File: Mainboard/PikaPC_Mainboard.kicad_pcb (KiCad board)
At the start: 2 copper layers, 190.5 x 147.3 mm, 67 parts, among them J10 Conn_01x08, J11 Conn_01x08, J12 Conn_01x08, J13 Conn_01x08, J14 Conn_01x08, J15 Conn_01x08, J16 Conn_01x08, J17 Conn_01x08, J18 Conn_01x10, J19 Conn_02x05_Odd_Even, J5 DIN41612_03x32_C_Split, J9 Conn_01x08, SW1 SW_Push_DPDT, SW2 SW_Push, U1 PPC403GA, U10 74LS07, U101 SN74LVC245A, U102 SN74LVC245A, U103 SN74LVC245A, U104 SN74LVC245A, U105 SN74LVC245A, U106 SN74LVC245A, U107 SN74LVC245A, U108 SN74LVC245A, U109 74LS244, U110 74LS244, U111 74LS244, U112 74LS244, U12 GD75232N, U13 74LVC125, U14 MCP120-315GI/TO, U15 AS6C4008-55PCN, U16 AS6C4008-55PCN, U2 ATF1508AS, U3 SST39VF010, U4 74AHCT244, U9 74LS04, Y1 25M, Y2 7M3728

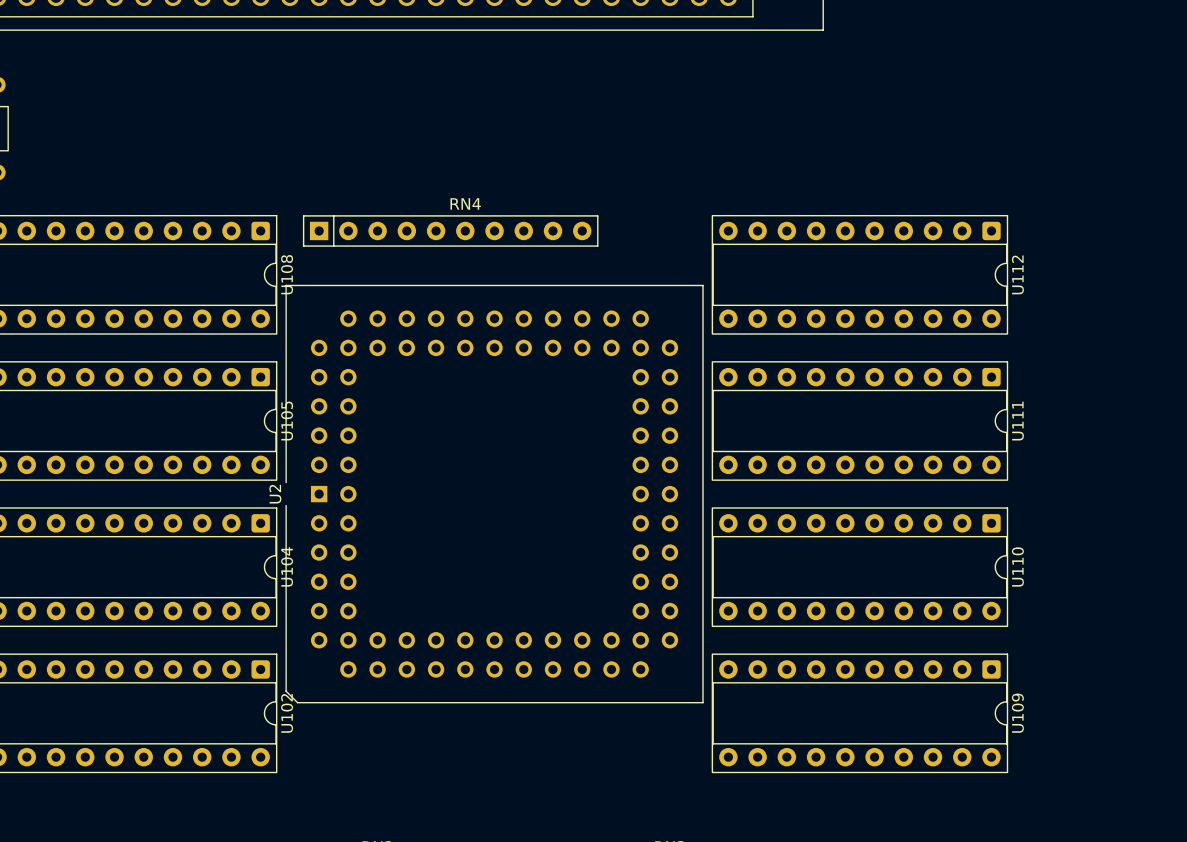
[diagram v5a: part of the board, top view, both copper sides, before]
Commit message: add pull-down resistors to AD bus
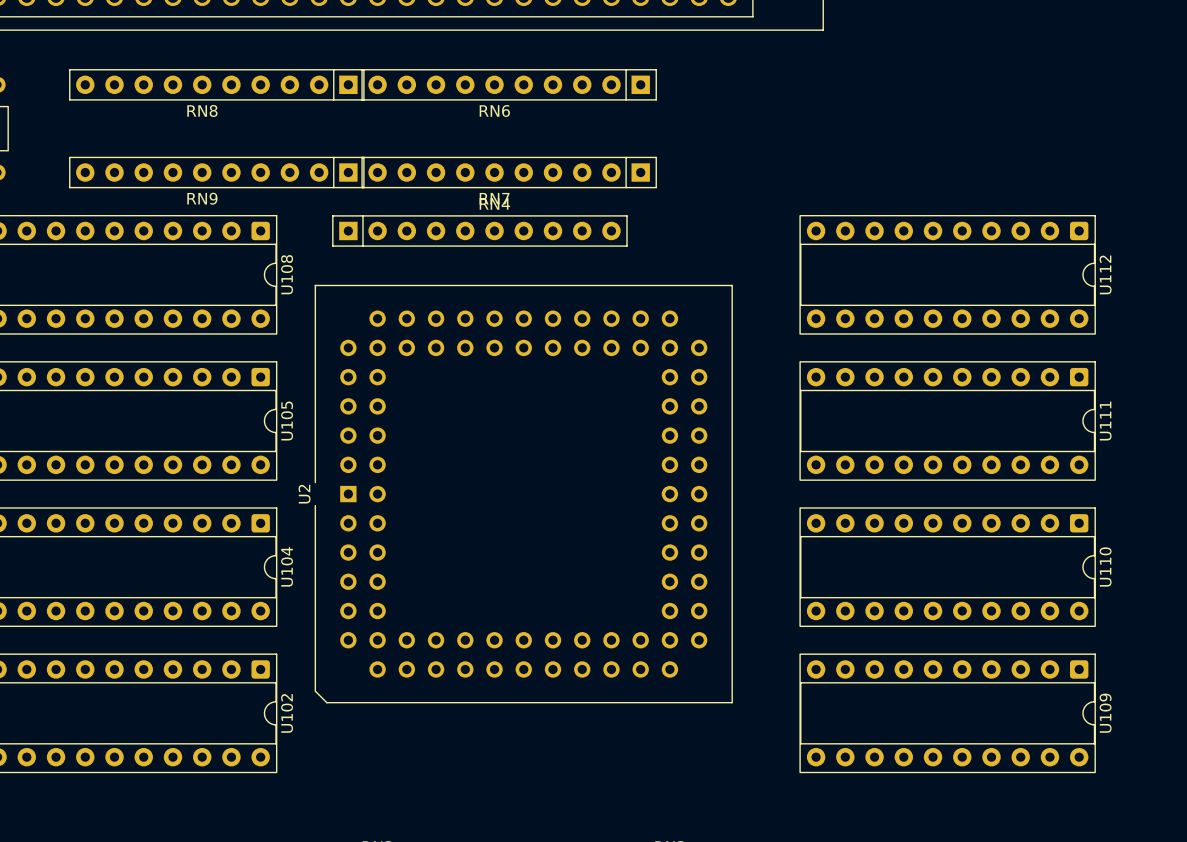
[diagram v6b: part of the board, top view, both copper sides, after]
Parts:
- added RN6: 10X-1-472LF, Resistor_THT:R_Array_SIP10, F.Cu at (165.1, 27.9)
- added RN7: 10X-1-472LF, Resistor_THT:R_Array_SIP10, F.Cu at (165.1, 35.6)
- added RN8: 10X-1-472LF, Resistor_THT:R_Array_SIP10, F.Cu at (139.7, 27.9)
- added RN9: 10X-1-472LF, Resistor_THT:R_Array_SIP10, F.Cu at (139.7, 35.6)
- moved U109 7.62 mm to (203.2, 78.7)
- moved U110 7.62 mm to (203.2, 66.0)
- moved U111 7.62 mm to (203.2, 53.3)
- moved U112 7.62 mm to (203.2, 40.6)
- moved RN4 2.54 mm to (139.7, 40.6)
- moved U2 2.54 mm to (139.7, 63.5)
